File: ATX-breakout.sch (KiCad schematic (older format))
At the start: 22 parts, among them J1 I2C, J10 3V3 out, J11 12V out, J2 EPS, J3 USB_A, J4 Raspberry_Pi_2_3, J5 ATX24pin, J6 12V out, J7 pson ext, J8 5V out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

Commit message: Finished up silkscreen
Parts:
- removed JP4: Voltage Select, Connector_PinHeader_2.54mm:PinHeader_1x03_P2.54mm_Vertical, symbol Jumper:Jumper_3_Open
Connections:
- net 3v3_rpi: now also R5.2, R6.1
- net SDA: now reaches J1.3 (Pin_3), J4.3 (SDA/GPIO2), R6.2
- net SCL: now reaches J1.4 (Pin_4), J4.5 (SCL/GPIO3), R5.1
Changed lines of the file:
@@
 	6975 2750 6925 2750
-Wire Wire Line
-	5300 2150 6250 2150
 Wire Wire Line
 	6925 2150 6925 2750
@@
 Wire Wire Line
 	6625 2650 6625 2700
-$Comp
-L Jumper:Jumper_3_Open JP4
-U 1 1 5CA26069
-P 6550 2475
-F 0 "JP4" H 6700 2375 50  0000 C CNN
-F 1 "Voltage Select" H 6550 2600 50  0000 C CNN
-F 2 "Connector_PinHeader_2.54mm:PinHeader_1x03_P2.54mm_Vertical" H 6550 2475 50  0001 C CNN
-F 3 "~" H 6550 2475 50  0001 C CNN
-	1    6550 2475
-	1    0    0    -1
-$EndComp
-Wire Wire Line
-	6800 2475 6850 2475
 Connection ~ 6850 2475
 Wire Wire Line
 	6850 2475 6850 2850
-Wire Wire Line
-	6300 2475 6250 2475
-Wire Wire Line
-	6250 2475 6250 2150
-Connection ~ 6250 2150
-Wire Wire Line
-	6250 2150 6925 2150
-Wire Wire Line
-	6550 2650 6550 2625
-Connection ~ 6550 2650
 Wire Wire Line
 	6200 2950 6625 2950
@@
 Wire Notes Line
 	8600 5300 10625 5300
+Text Label 6300 3050 0    50   ~ 0
+SCL
+Text Label 6300 2950 0    50   ~ 0
+SDA
+Wire Wire Line
+	5300 2150 6925 2150
+Wire Wire Line
+	6625 2650 6625 2475
+Wire Wire Line
+	6625 2475 6850 2475
+Connection ~ 6625 2650
 $EndSCHEMATC

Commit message: Switched to a more common transistor pinout
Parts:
- Q1: symbol Device:Q_NPN_BCE -> Device:Q_NPN_EBC
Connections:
- net GND: now also Q1.1 (E); no longer Q1.3 (E)
- net at JP3.3 (B): now also Q1.3 (C); no longer Q1.2 (C)
- net at R3.1, R4.2: now also Q1.2 (B); no longer Q1.1 (B)
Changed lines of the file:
@@
 	8500 2725 8575 2725
 $Comp
-L Device:Q_NPN_BCE Q1
+L Device:Q_NPN_EBC Q1
 U 1 1 5C91A39E
 P 8250 3200
@@
 	-1   0    0    -1
 $EndComp
-Wire Wire Line
-	8000 3150 8000 3200
 Connection ~ 8000 3200
 Wire Wire Line

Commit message: Added third 12v connector, fixed 12v-5v short
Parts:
- added J12: 12V out, Connector_Phoenix_MSTB:PhoenixContact_MSTBA_2,5_2-G_1x02_P5.00mm_Horizontal, symbol Connector:Screw_Terminal_01x02
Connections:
- net +12V: now also J12.2 (Pin_2)
- net GND: now also J12.1 (Pin_1)
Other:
- moved on the sheet: J10, J11, J6, J8, J9

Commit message: added schematic PDF and updated BOM
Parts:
- R2: value 10K -> 10k
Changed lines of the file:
@@
 P 4275 3175
 F 0 "R2" H 4217 3129 50  0000 R CNN
-F 1 "10K" H 4217 3220 50  0000 R CNN
+F 1 "10k" H 4217 3220 50  0000 R CNN
 F 2 "Resistor_THT:R_Axial_DIN0207_L6.3mm_D2.5mm_P7.62mm_Horizontal" H 4275 3175 50  0001 C CNN
 F 3 "~" H 4275 3175 50  0001 C CNN

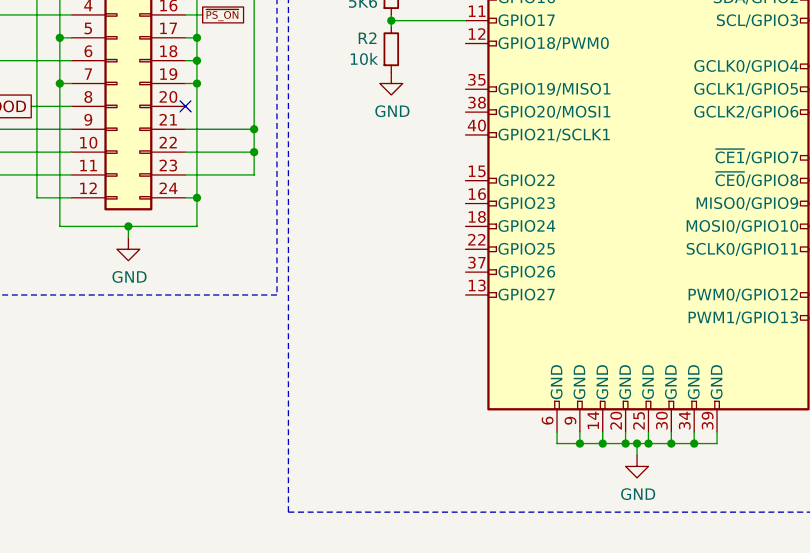
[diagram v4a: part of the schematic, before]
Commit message: rotated EPS and improved ground routing
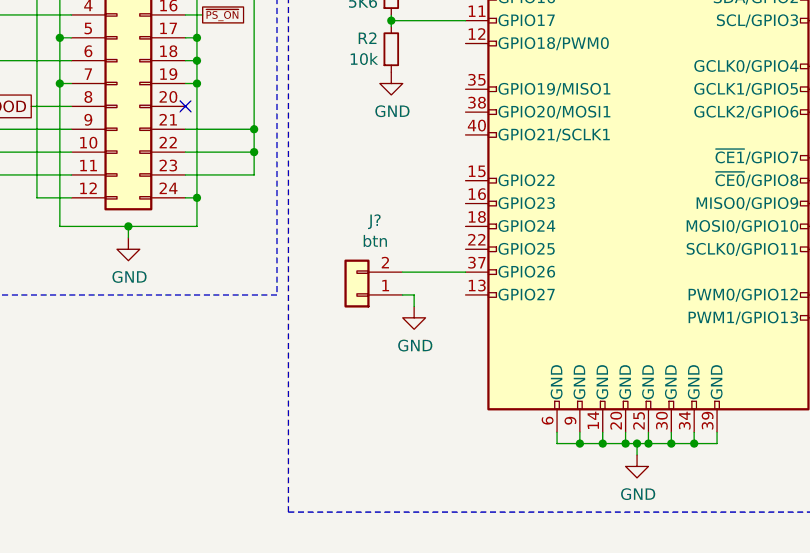
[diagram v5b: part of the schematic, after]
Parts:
- added J?: btn, Connector_PinHeader_2.54mm:PinHeader_1x02_P2.54mm_Vertical, symbol Connector_Generic:Conn_01x02
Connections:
- net GND: now also J?.1 (Pin_1)
- net at J4.37 (GPIO26): now also J?.2 (Pin_2)
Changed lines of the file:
@@
 Wire Wire Line
 	10000 3425 10050 3425
+$Comp
+L Connector_Generic:Conn_01x02 J?
+U 1 1 5CAD6096
+P 4125 4250
+F 0 "J?" H 4045 3925 50  0000 C CNN
+F 1 "btn" H 4045 4016 50  0000 C CNN
+F 2 "Connector_PinHeader_2.54mm:PinHeader_1x02_P2.54mm_Vertical" H 4125 4250 50  0001 C CNN
+F 3 "~" H 4125 4250 50  0001 C CNN
+	1    4125 4250
+	-1   0    0    1
+$EndComp
+Wire Wire Line
+	4325 4150 4600 4150
+Wire Wire Line
+	4325 4250 4375 4250
+Wire Wire Line
+	4375 4250 4375 4300
+$Comp
+L power:GND #PWR?
+U 1 1 5CAEFDE2
+P 4375 4300
+F 0 "#PWR?" H 4375 4050 50  0001 C CNN
+F 1 "GND" H 4380 4127 50  0000 C CNN
+F 2 "" H 4375 4300 50  0001 C CNN
+F 3 "" H 4375 4300 50  0001 C CNN
+	1    4375 4300
+	1    0    0    -1
+$EndComp
 $EndSCHEMATC

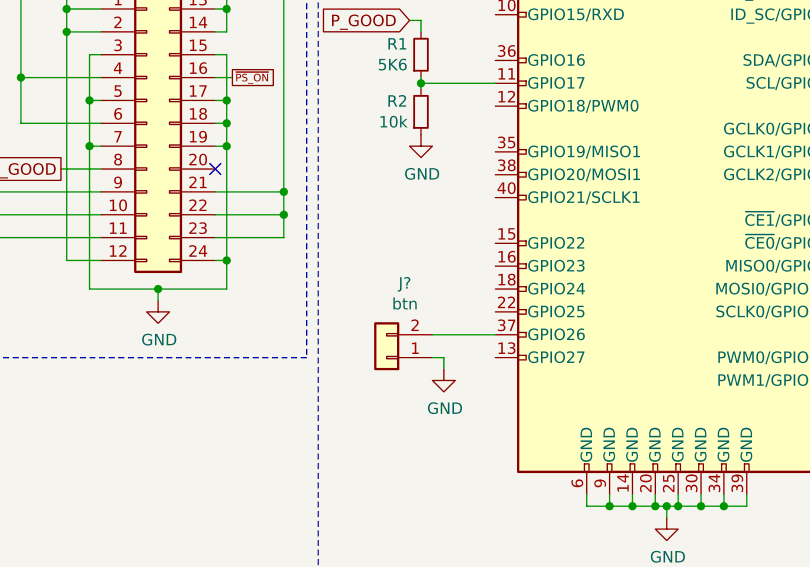
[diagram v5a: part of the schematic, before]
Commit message: Updated pdf and readme
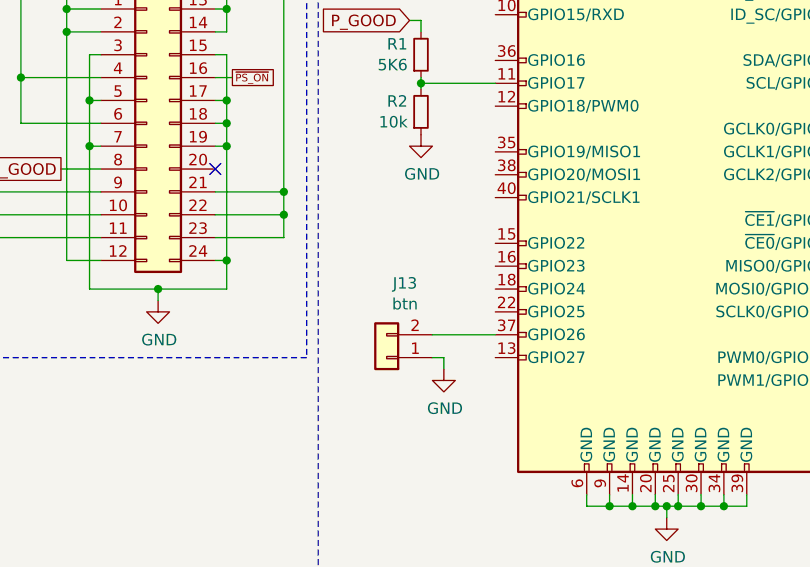
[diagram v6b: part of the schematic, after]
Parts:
- gave numbers to parts that had none: 1
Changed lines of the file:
@@
 	10000 3425 10050 3425
 $Comp
-L Connector_Generic:Conn_01x02 J?
+L Connector_Generic:Conn_01x02 J13
 U 1 1 5CAD6096
 P 4125 4250
-F 0 "J?" H 4045 3925 50  0000 C CNN
+F 0 "J13" H 4045 3925 50  0000 C CNN
 F 1 "btn" H 4045 4016 50  0000 C CNN
 F 2 "Connector_PinHeader_2.54mm:PinHeader_1x02_P2.54mm_Vertical" H 4125 4250 50  0001 C CNN
@@
 	4375 4250 4375 4300
 $Comp
-L power:GND #PWR?
+L power:GND #PWR0134
 U 1 1 5CAEFDE2
 P 4375 4300
-F 0 "#PWR?" H 4375 4050 50  0001 C CNN
+F 0 "#PWR0134" H 4375 4050 50  0001 C CNN
 F 1 "GND" H 4380 4127 50  0000 C CNN
 F 2 "" H 4375 4300 50  0001 C CNN

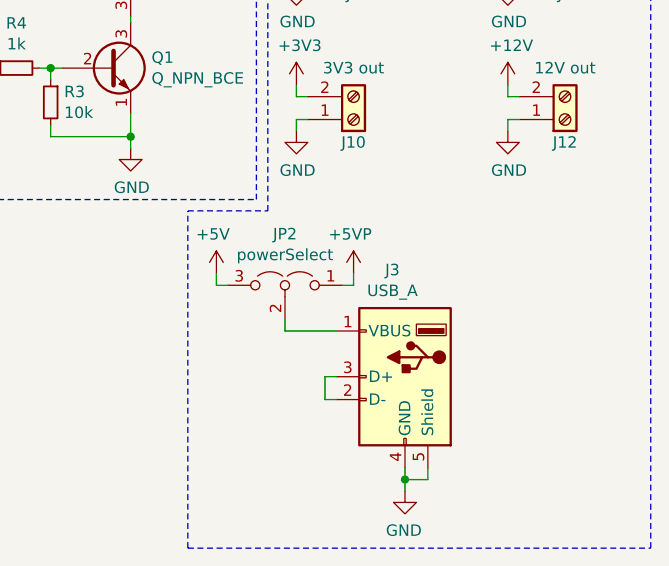
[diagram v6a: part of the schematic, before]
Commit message: Switched to vertical USB to clear pi ethernet jack
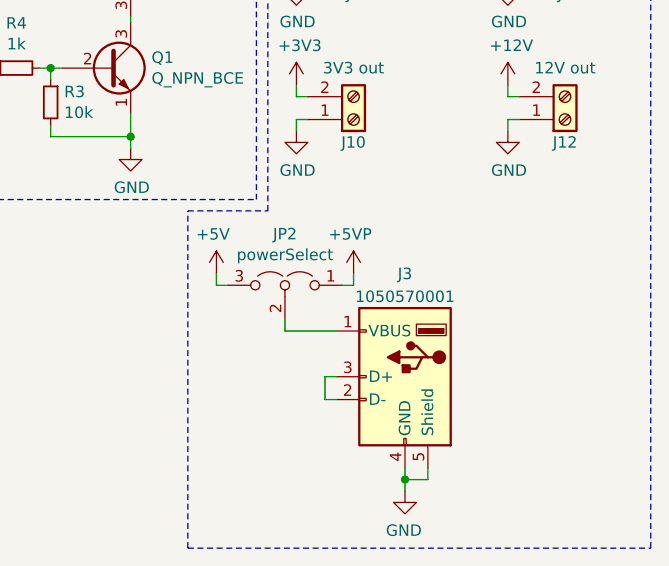
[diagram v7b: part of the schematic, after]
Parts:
- J3: value USB_A -> 1050570001; footprint Connector_USB:USB_A_Stewart_SS-52100-001_Horizontal -> Connector_USB:USB_A_Molex_105057_Vertical
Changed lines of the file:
@@
 U 1 1 5C7EDB1E
 P 9550 4550
-F 0 "J3" H 9605 5017 50  0000 C CNN
-F 1 "USB_A" H 9605 4926 50  0000 C CNN
-F 2 "Connector_USB:USB_A_Stewart_SS-52100-001_Horizontal" H 9700 4500 50  0001 C CNN
+F 0 "J3" H 9550 5000 50  0000 C CNN
+F 1 "1050570001" H 9550 4900 50  0000 C CNN
+F 2 "Connector_USB:USB_A_Molex_105057_Vertical" H 9700 4500 50  0001 C CNN
 F 3 " ~" H 9700 4500 50  0001 C CNN
 	1    9550 4550
